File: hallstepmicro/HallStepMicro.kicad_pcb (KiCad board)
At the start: 2 copper layers, 32 parts, among them IC1 ATTINY84A-SS, K1 CONN_3, K2 CONN_3, K3 CONN_3, K4 CONN_3

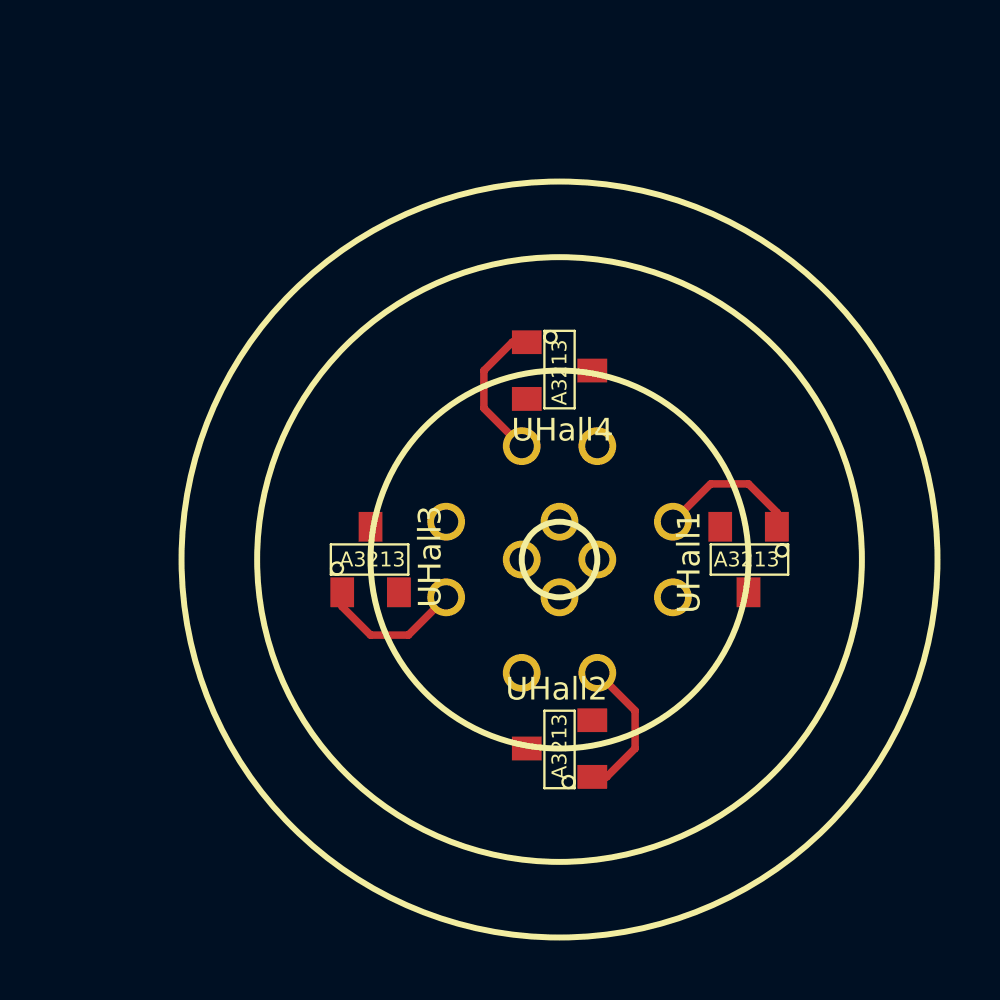
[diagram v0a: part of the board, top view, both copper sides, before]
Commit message: Added keepouts, fill and grew TO-92HL
Created TO-92HL (long) for mask showing larger placement area.
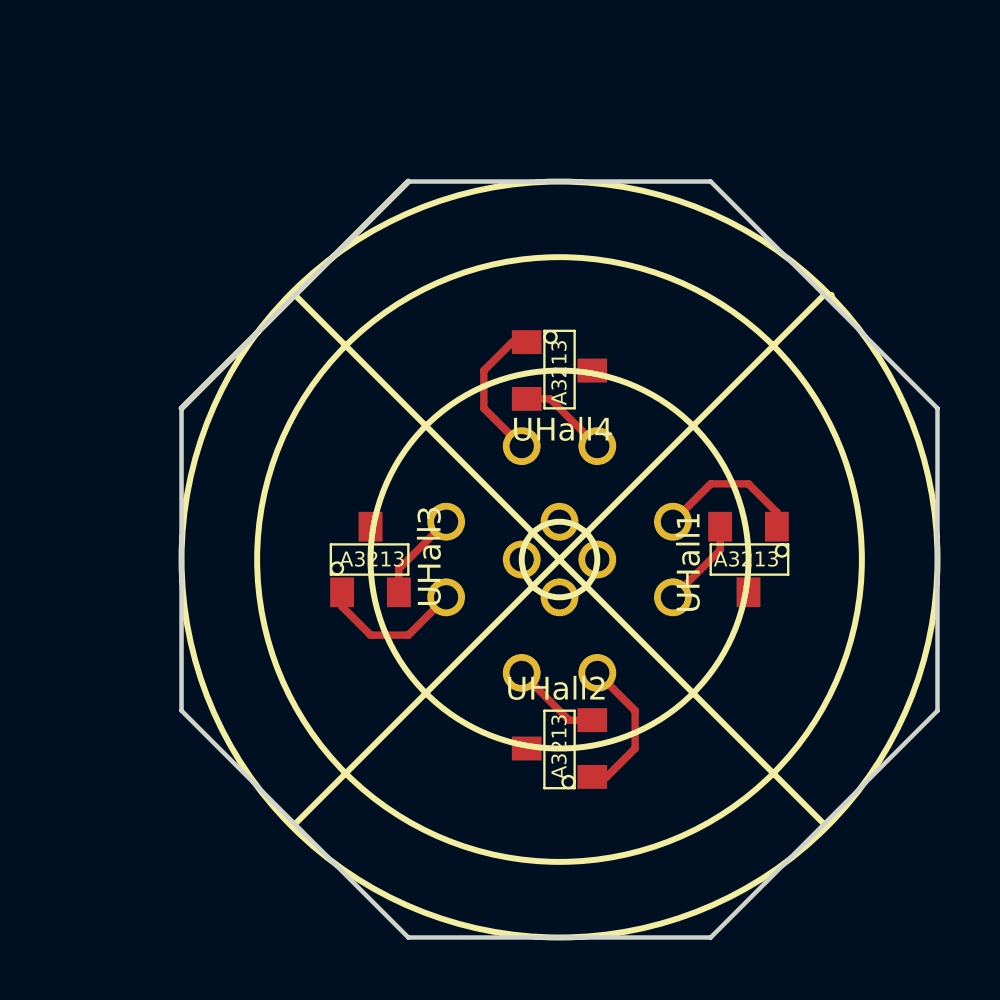
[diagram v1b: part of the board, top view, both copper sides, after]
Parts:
- K1, K2, K3, K4: footprint TO92H -> TO92HL
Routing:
- net /HallSensors1/hall4: track 0.00 -> 3.03 mm
- net /HallSensors1/hall1: track 0.00 -> 3.03 mm
- net /HallSensors1/hall3: track 0.00 -> 3.03 mm
- net /HallSensors1/hall2: track 0.00 -> 3.03 mm
- added copper zone on B.Cu, net VCC
- added copper zone on F.Cu, net VSS
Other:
- board outline added: 25.4 x 25.4 mm

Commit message: Working on layout.
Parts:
- JHALLS1: moved to B.Cu
- moved JHALLS1 181.0 mm to (151.1, 76.2), turned to 90 degrees
- moved CH1 168.1 mm to (133.3, 80.0), turned to 180 degrees
- moved HALL6OUT1 163.2 mm to (141.6, 76.2), turned to 90 degrees
- moved HALL6IN1 151.8 mm to (128.3, 54.6), turned to 180 degrees
- moved CH4 141.0 mm to (130.8, 69.8), turned to 270 degrees
- moved DCM1 139.2 mm to (115.6, 48.3), turned to 90 degrees
- moved CH2 137.0 mm to (123.2, 82.5), turned to 90 degrees
- moved CH3 136.2 mm to (120.7, 72.4)
- moved STEPIN1 134.4 mm to (141.0, 49.5), turned to 90 degrees
- moved IC1 129.1 mm to (128.3, 48.3), turned to 180 degrees
- moved CD2 125.5 mm to (130.8, 82.5), turned to 90 degrees
- moved CD1 121.8 mm to (133.3, 72.4), turned to 180 degrees
- moved JSTEP1 120.0 mm to (136.5, 47.0), turned to 90 degrees
- moved CD4 119.4 mm to (123.2, 69.8), turned to 270 degrees
- moved RPHASE1 118.7 mm to (133.3, 41.9), turned to 270 degrees
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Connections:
- JDC1 pad 3: /PWM -> /MODE
- JDC1 pad 4: /DC_ENABLE -> /DC_MODE
- JDC1 pad 7: /MODE -> /PWM
- JDC1 pad 8: /DC_MODE -> /DC_ENABLE
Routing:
- net /HallSensors1/hall3: track 3.03 -> 28.1 mm, vias 0 -> 1
- net /HallSensors1/hall2: track 3.03 -> 25.6 mm
- net /HallSensors1/hall4: track 3.03 -> 18.8 mm
- net /HallSensors1/hall1: track 3.03 -> 16.3 mm, vias 0 -> 1
- net VCC: track 19.6 -> 32.3 mm, vias 0 -> 12
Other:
- board size 25.4 x 25.4 mm -> 29.8 x 25.4 mm
- net class PWR added: clearance 0.254, trace_width 0.508, via_dia 0.889, via_drill 0.635

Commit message: Simplify. Simplify. Simplify.
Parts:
- removed JDC1: CONN_4X2, GS_4x2
- removed JHALLS1: CONN_6X2, GS_6x2
- removed JSTEP1: CONN_5X2, GS_5x2
- removed K1, K2, K3, K4: CONN_3, TO92HL
- added RDIR1: 0.0, SM0805, F.Cu at (132.1, 50.8)
- moved ISP6PIN1 11.5 mm to (128.3, 39.4)
- moved RMODE1 8.89 mm to (121.9, 41.9)
- moved CD4 6.99 mm to (130.2, 69.8)
- moved CD1 6.98 mm to (133.3, 79.4)
- moved CD2 6.98 mm to (123.8, 82.5)
- moved CD3 6.98 mm to (120.7, 73.0)
- moved RENB1 6.35 mm to (119.4, 41.9)
- moved RESET1 5.68 mm to (135.9, 39.4), turned to 270 degrees
- moved RRESET1 5.68 mm to (133.3, 39.4)
- moved RPHASE1 5.24 mm to (132.1, 47.0)
- moved CH3 5.21 mm to (124.2, 76.2), turned to 90 degrees
- moved CH1 5.21 mm to (129.8, 76.2), turned to 270 degrees
- moved CH4 5.04 mm to (127.0, 73.2), turned to 0 degrees
- moved CH2 5.04 mm to (127.0, 79.2), turned to 180 degrees
- moved SENSE1 4.02 mm to (118.1, 38.1)
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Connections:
- IC1 pad 2: /ENB -> /STP_ENB
- IC1 pad 3: /MODE -> /DC_MODE
- IC1 pad 5: /PWM -> /DC_ENABLE
- IC1 pad 7: /MOSI -> /STP_MAX
- IC1 pad 8: /MISO -> /STP_MIN
- IC1 pad 9: /SCK -> /STP_STEP
- ISP6PIN1 pad 1: /MISO -> /STP_MIN
- ISP6PIN1 pad 3: /SCK -> /STP_STEP
- ISP6PIN1 pad 4: /MOSI -> /STP_MAX
- RBRK1 pad 2: /BRAKE -> /DC_BRAKE
- RENB1 pad 2: /PWM -> /DC_ENABLE
- RMODE1 pad 2: /MODE -> /DC_MODE
- RPHASE1 pad 2: /PHASE_DIR -> /DC_PHASE
- STEPIN1 pad 5: /STP_ENABLE -> /STP_ENB
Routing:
- net VSS: track 0.00 -> 42.9 mm, vias 0 -> 4
- net VCC: track 32.3 -> 14.5 mm, vias 12 -> 8
- net /HallSensors1/hall2: track 25.6 -> 18.0 mm, vias 0 -> 1
- net /HallSensors1/hall3: track 28.1 -> 22.0 mm, vias 1 -> 0
- net /HallSensors1/hall1: track 16.3 -> 14.3 mm, vias 1 -> 0
- net /HallSensors1/hall4: track 18.8 -> 19.6 mm, vias 0 -> 1
- added copper zone on F.Cu, net GND
- added copper zone on B.Cu, net VDD
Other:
- board size 29.8 x 25.4 mm -> 34.3 x 55.9 mm

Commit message: Cleaned up keepouts.
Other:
- board size 34.3 x 55.9 mm -> 33 x 55.9 mm

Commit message: More workin' the layout.
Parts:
- moved RESET1 20.3 mm to (115.6, 39.4), turned to 180 degrees
- moved DCM1 17.8 mm to (133.3, 49.5)
- moved STEPIN1 14.9 mm to (123.2, 54.6), turned to 0 degrees
- moved RBRK1 13.3 mm to (130.8, 54.6), turned to 90 degrees
- moved HALL6IN1 12.5 mm to (114.3, 49.5), turned to 90 degrees
- moved RENB1 11.4 mm to (130.2, 45.7), turned to 0 degrees
- moved RMODE1 7.18 mm to (127.0, 47.0)
- moved IC1 6.63 mm to (119.4, 46.4), turned to 90 degrees
- moved SENSE1 2.84 mm to (116.8, 35.6), turned to 0 degrees
- moved ISP6PIN1 2.54 mm to (128.3, 36.8)
- moved RPHASE1 2.29 mm to (130.2, 48.3), turned to 0 degrees
- moved RDIR1 1.91 mm to (130.2, 50.8), turned to 0 degrees
- moved RRESET1 1.90 mm to (133.3, 37.5)
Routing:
- net /STP_STEP: track 0.00 -> 27.8 mm, vias 0 -> 1
- net /STP_MIN: track 0.00 -> 27.0 mm
- net /RESET: track 0.00 -> 25.1 mm, vias 0 -> 2
- net /STP_MAX: track 0.00 -> 25.0 mm, vias 0 -> 1
- net VDD: track 0.00 -> 17.0 mm, vias 0 -> 2
- net /DC_MODE: track 0.00 -> 14.5 mm, vias 0 -> 1
- net /DC_ENABLE: track 0.00 -> 12.0 mm
- net /STP_DIR: track 0.00 -> 10.4 mm, vias 0 -> 1
- net /SENSE: track 0.00 -> 10.3 mm, vias 0 -> 1
- net /STP_ENB: track 0.00 -> 9.19 mm
- net /DC_PHASE: track 0.00 -> 4.76 mm
- net /hall4_in: track 0.00 -> 3.33 mm
- net /hall1_in: track 0.00 -> 3.33 mm
- net /hall3_in: track 0.00 -> 2.80 mm
- net /hall2_in: track 0.00 -> 2.80 mm
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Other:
- outline, holes or cut-outs redrawn

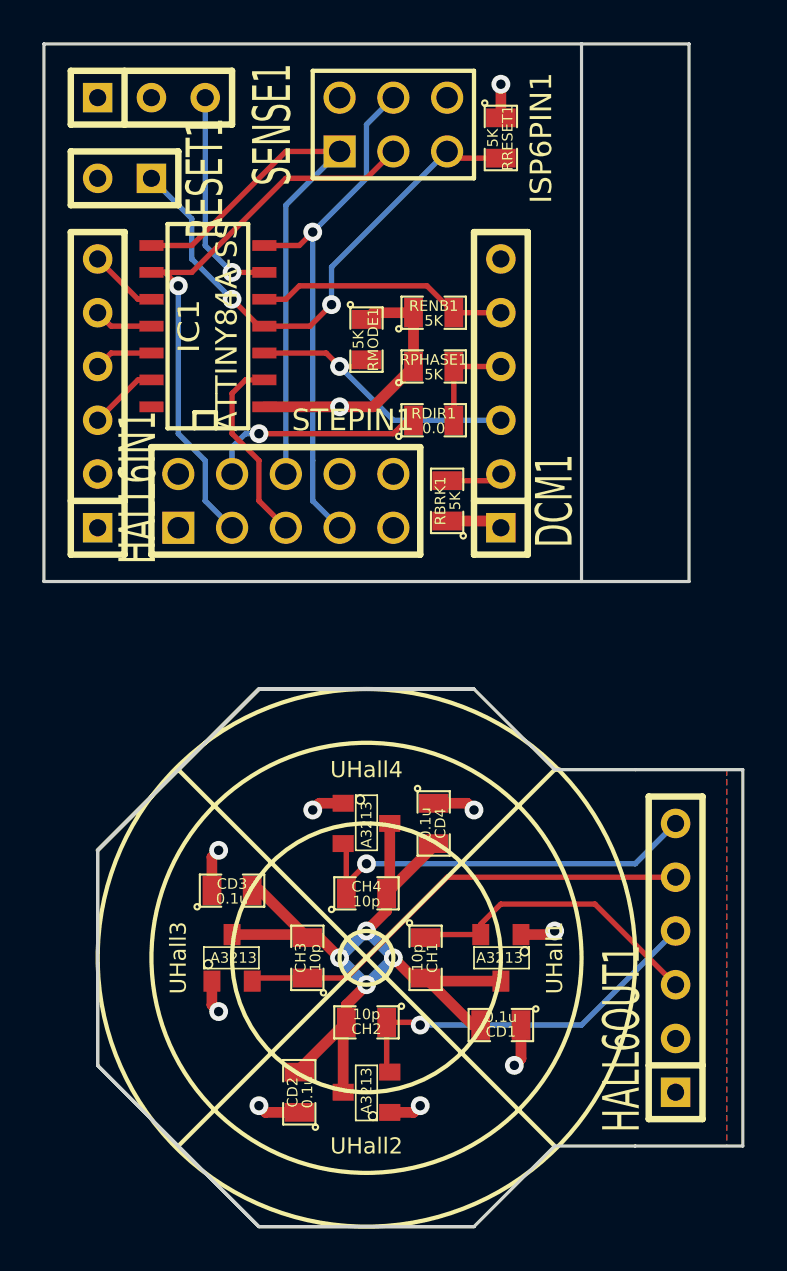
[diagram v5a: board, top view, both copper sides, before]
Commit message: Modified 3+ pin headers to offset pins +/-0.005"
Using SparkFun trick to offset pin holes to make headers more secure.
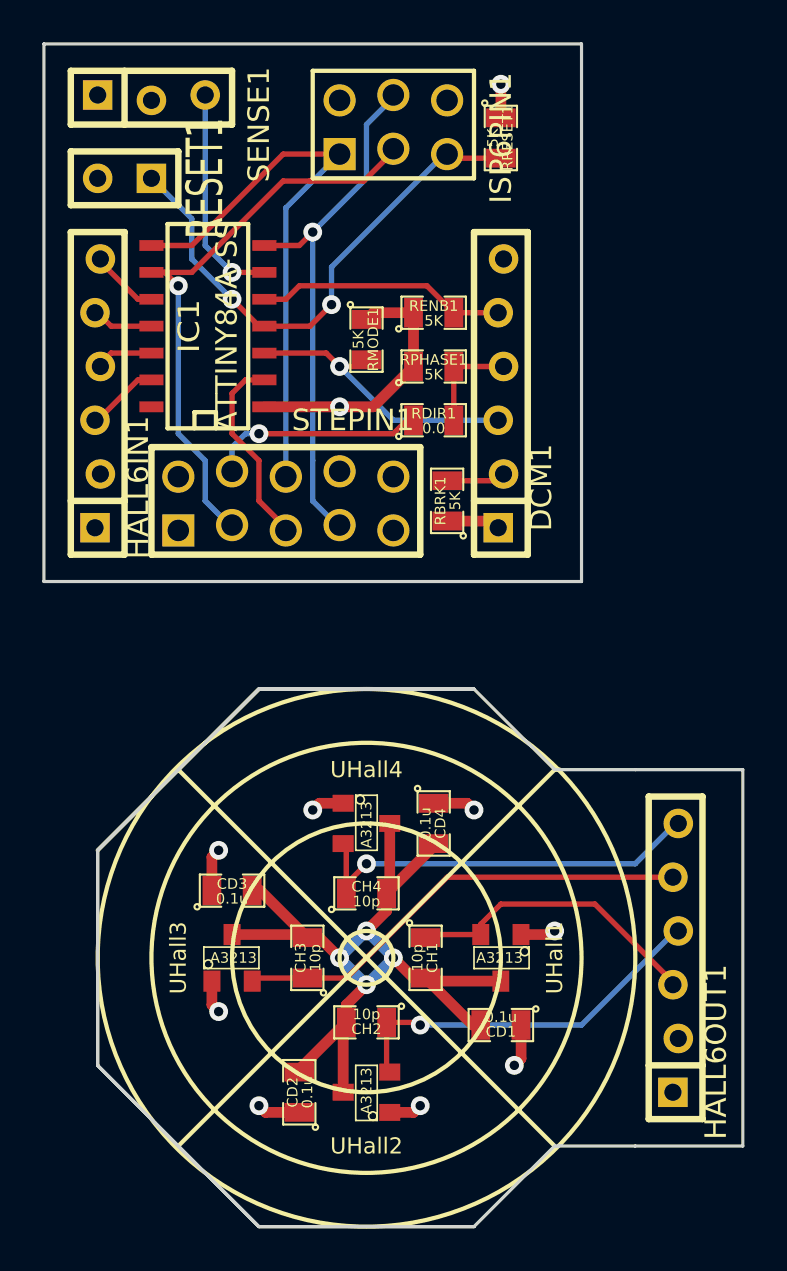
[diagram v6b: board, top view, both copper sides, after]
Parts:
- DCM1, HALL6IN1, HALL6OUT1: footprint SIL-6 -> SIL6-offset-0p005
- ISP6PIN1: footprint pin_array_3x2 -> pin_array_3x2-offset-0p005
- SENSE1: footprint SIL-3 -> SIL3-offset-0p005
- STEPIN1: footprint PIN_ARRAY_5x2 -> PIN_ARRAY_5x2-offset-0p005
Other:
- outline, holes or cut-outs redrawn

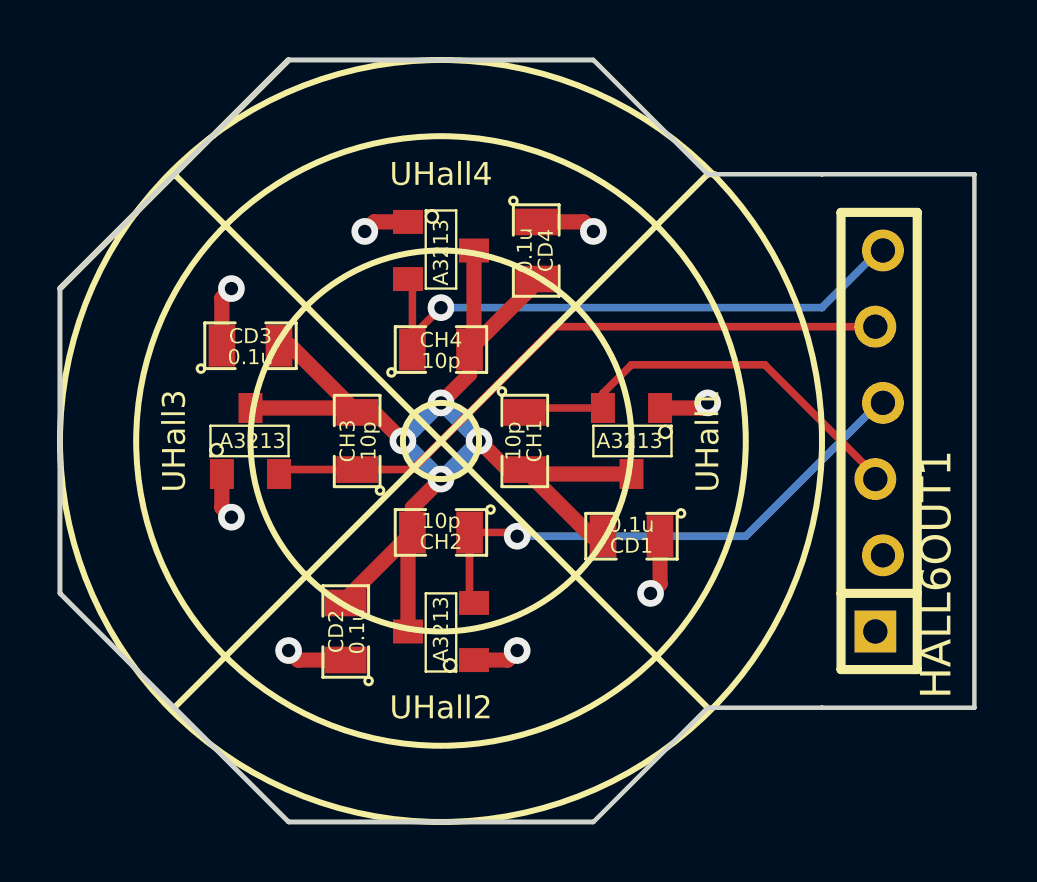
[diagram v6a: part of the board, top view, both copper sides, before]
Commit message: Cleaned up routing on sensor mount.
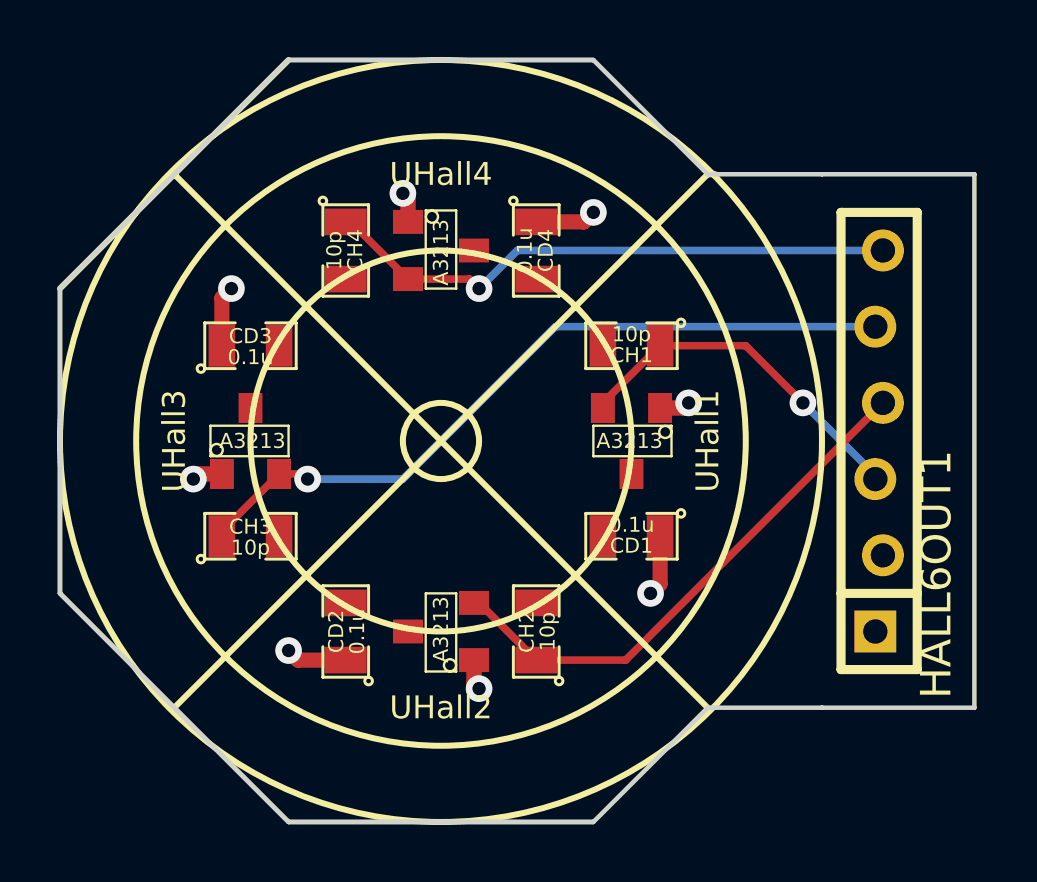
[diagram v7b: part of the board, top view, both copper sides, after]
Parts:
- moved CH3 4.77 mm to (120.7, 79.4), turned to 0 degrees
- moved CH1 4.77 mm to (133.3, 73.0), turned to 180 degrees
- moved CH4 4.58 mm to (123.8, 69.8), turned to 270 degrees
- moved CH2 4.58 mm to (130.2, 82.5), turned to 90 degrees
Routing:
- net VSS: track 42.9 -> 0.32 mm, vias 4 -> 0
- net /HallSensors1/hall3: track 22.0 -> 24.9 mm, vias 0 -> 1
- net /HallSensors1/hall1: track 14.3 -> 12.0 mm, vias 0 -> 1
- net VCC: track 14.5 -> 12.2 mm
- net /HallSensors1/hall2: vias 1 -> 0
